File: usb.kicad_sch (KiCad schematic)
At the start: 20 parts, among them J201 1054500101, Q201 S8050, Q202 S8050, U201 CH340G, U202 CP2104, Y201 Crystal_GND24

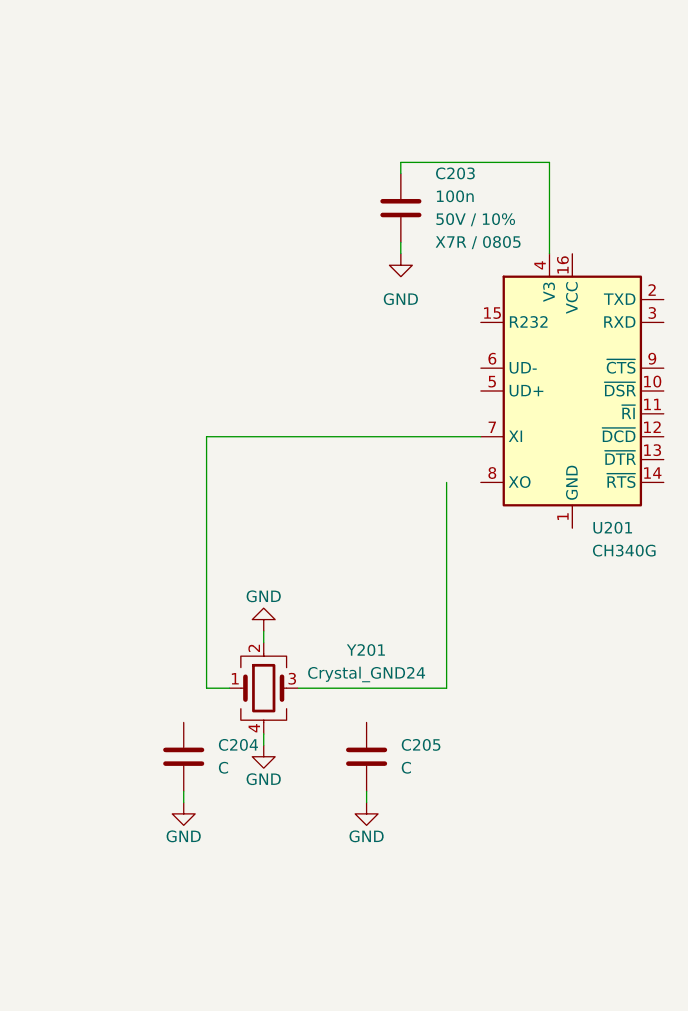
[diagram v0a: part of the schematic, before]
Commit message: Remove CH340G
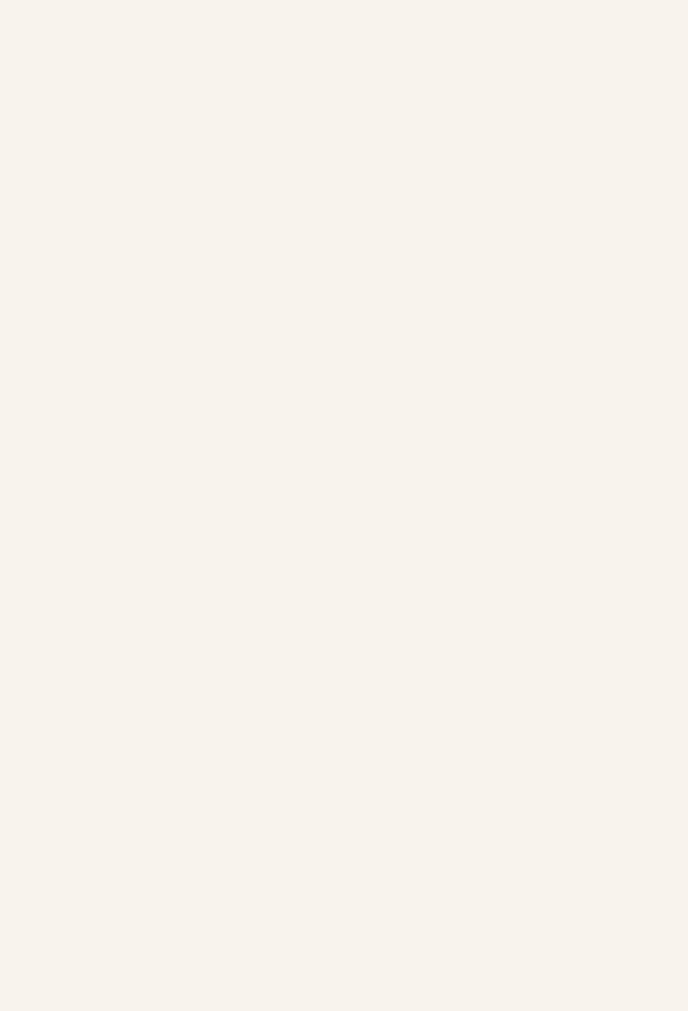
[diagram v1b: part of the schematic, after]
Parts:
- removed C203: 100n, Capacitor_SMD:C_0805_2012Metric, symbol Device:C
- removed C204, C205: C, symbol Device:C
- removed U201: CH340G, Package_SO:SOIC-16_3.9x9.9mm_P1.27mm, symbol Interface_USB:CH340G
- removed Y201: Crystal_GND24, symbol Device:Crystal_GND24

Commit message: Switch to 16 pin USB-C
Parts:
- removed C207: 4u7, Capacitor_SMD:C_0805_2012Metric, symbol Device:C_Small
- C201, C202, C208: symbol Device:C -> Device:C_Small
- J201: value 1054500101 -> GT-USB-7010ASV; footprint busbuddy:USB_C_Receptacle_Molex_105450-0101 -> busbuddy:USB_C_Receptacle_G-Switch_GT-USB-7010ASV; LCSC Part Number C134092 -> C2988369; MPN MOLEX -> G-Switch; Manufacturer 1054500101 -> GT-USB-7010ASV
- R201, R202, R203, R204: symbol Device:R -> Device:R_Small
- R205: footprint (none) -> Resistor_SMD:R_0805_2012Metric
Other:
- moved on the sheet: Q201, R201, R202, R203, R204

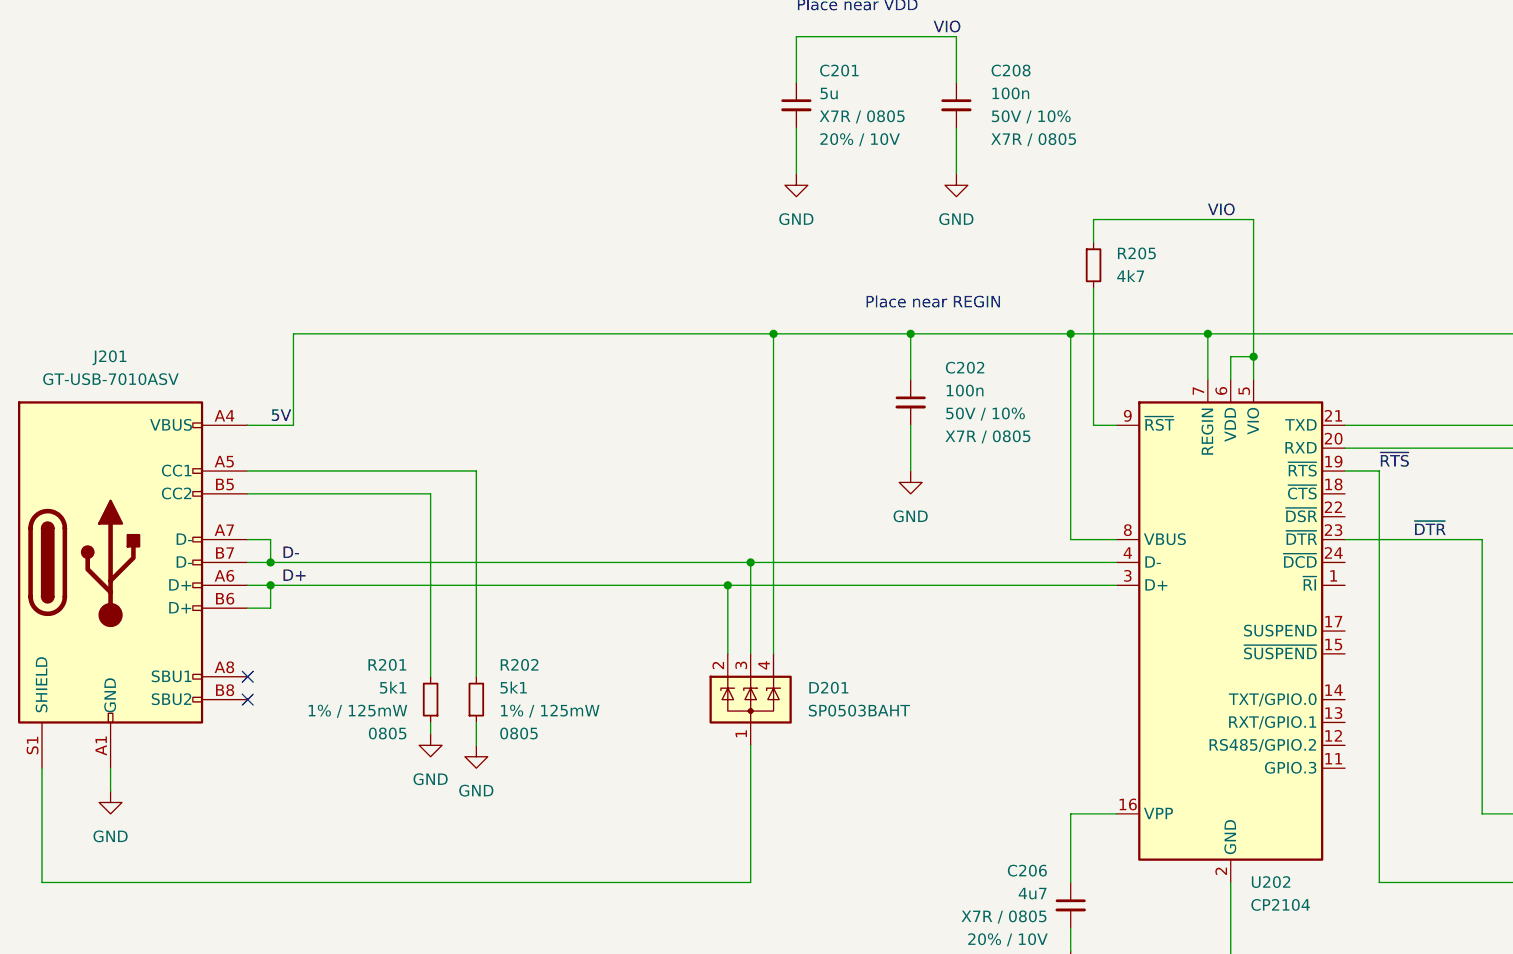
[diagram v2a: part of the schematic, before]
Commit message: Correct SPI pinout
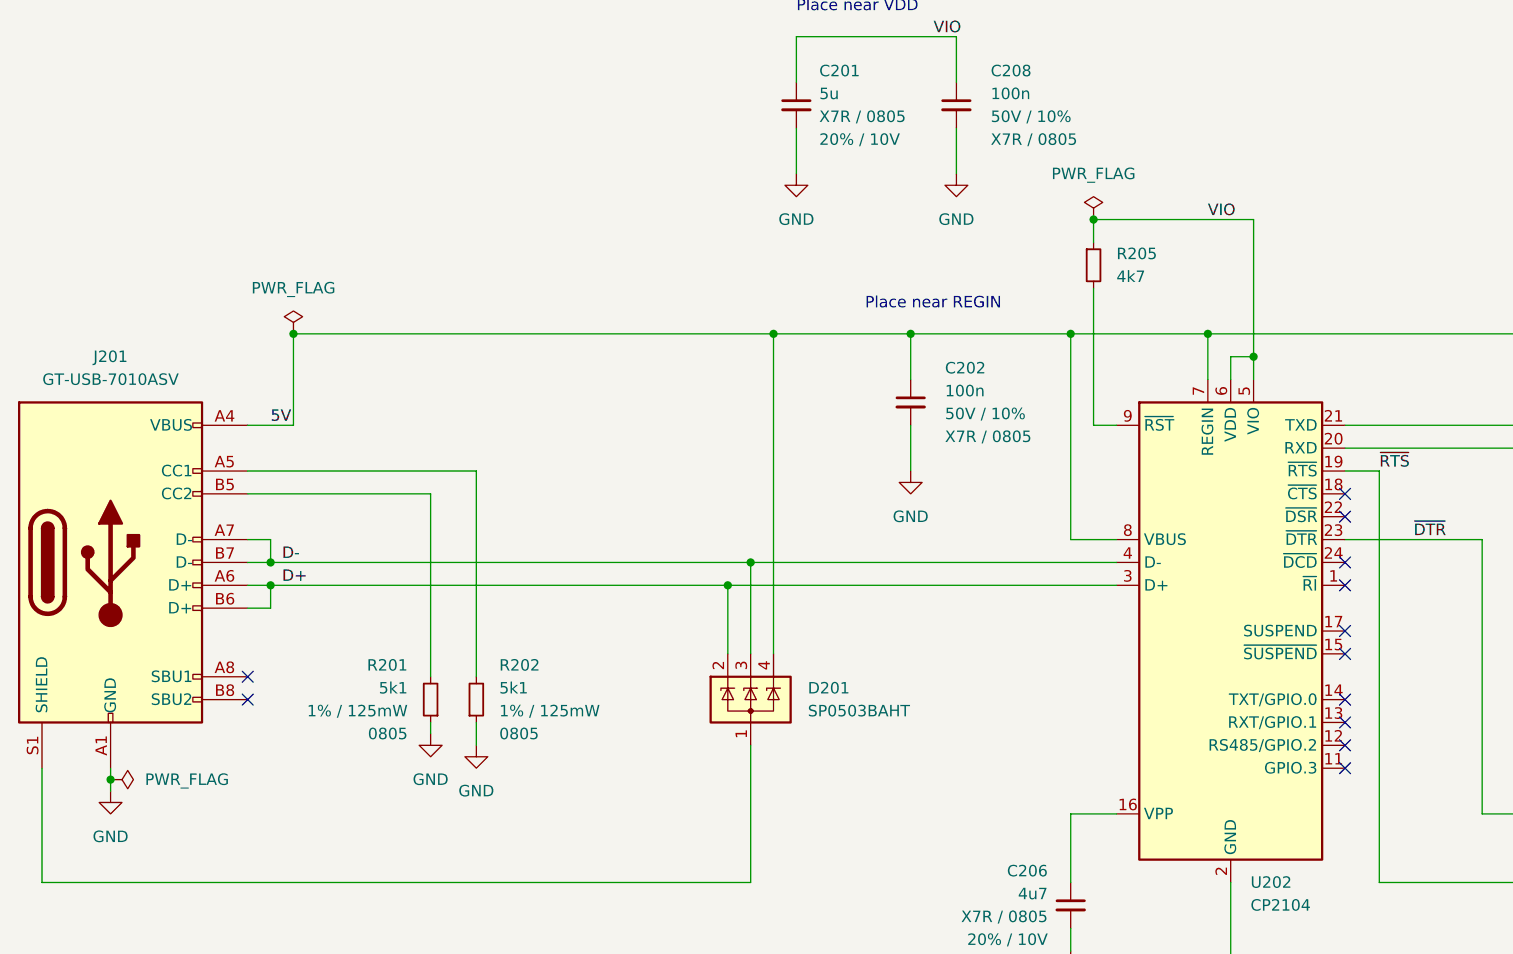
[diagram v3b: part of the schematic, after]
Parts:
- J201: symbol Connector:USB_C_Receptacle_USB2.0 -> Connector:USB_C_Receptacle_USB2.0_16P
- Q201, Q202: footprint Package_TO_SOT_SMD:SOT-23 -> Package_TO_SOT_SMD:SOT-23-3
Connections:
- no-connect marks 2 -> 12

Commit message: Finish everything
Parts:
- C201: value 5u -> 4u7; LCSC Part Number C5189822 -> C98192; MPN CS2012X7R106M100NRE -> CL21A475KBQNNNE; Manufacturer Samwha Capacitor -> Samsung Electro-Mechanics; Rated Voltage 10V -> 50V; Tolerance 20% -> 10%
- C206: LCSC Part Number C5189822 -> C98192; MPN CS2012X7R106M100NRE -> CL21A475KBQNNNE; Manufacturer Samwha Capacitor -> Samsung Electro-Mechanics; Rated Voltage 10V -> 50V; Tolerance 20% -> 10%
- D201: LCSC Part Number (none) -> C7074; MPN (none) -> SP0503BAHTG; Manufacturer (none) -> Littelfuse
- R205: LCSC Part Number (none) -> C17673; MPN (none) -> 0805W8F4701T5E; Manufacturer (none) -> UNI-ROYAL(Uniroyal Elec)
- U202: LCSC Part Number (none) -> C47742; MPN (none) -> CP2104-F03-GMR; Manufacturer (none) -> SKYWORKS/SILICON LABS
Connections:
- net D+: now also D201.3 (K); no longer D201.2 (K)
- net D-: now also D201.2 (K); no longer D201.3 (K)
- net CC1: now reaches J201.A5 (CC1), R202.2
- net CC2: now reaches J201.B5 (CC2), R201.2
- net SHIELD: now reaches D201.1 (A), J201.S1 (SHIELD)
- net CP2104_~{RST}: now reaches R205.2, U202.9 (~{RST})
- net VPP: now reaches C206.1, U202.16 (VPP)

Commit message: Rename project
Damn squatters
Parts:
- J201: footprint busbuddy:USB_C_Receptacle_G-Switch_GT-USB-7010ASV -> youdbetterrun:USB_C_Receptacle_G-Switch_GT-USB-7010ASV
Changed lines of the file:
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@@
 		)
 		(instances
-			(project "busbuddy"
+			(project "youdbetterrun"
 				(path "/50da2b4e-34b1-4787-8ee6-5d7d17f804f4/951b5697-f1e3-4d2e-841e-7032f41eb35f"
 					(reference "#FLG03")
@@
 			)
 		)
-		(property "Footprint" "busbuddy:USB_C_Receptacle_G-Switch_GT-USB-7010ASV"
+		(property "Footprint" "youdbetterrun:USB_C_Receptacle_G-Switch_GT-USB-7010ASV"
 			(at 54.61 76.2 0)
 			(effects
@@
 		)
 		(instances
-			(project "busbuddy"
+			(project "youdbetterrun"
 				(path "/50da2b4e-34b1-4787-8ee6-5d7d17f804f4/951b5697-f1e3-4d2e-841e-7032f41eb35f"
 					(reference "J201")
@@
 		)
 		(instances
-			(project "busbuddy"
+			(project "youdbetterrun"
 				(path "/50da2b4e-34b1-4787-8ee6-5d7d17f804f4/951b5697-f1e3-4d2e-841e-7032f41eb35f"
 					(reference "Q202")
@@
 		)
 		(instances
-			(project "busbuddy"
+			(project "youdbetterrun"
 				(path "/50da2b4e-34b1-4787-8ee6-5d7d17f804f4/951b5697-f1e3-4d2e-841e-7032f41eb35f"
 					(reference "R202")
@@
 		)
 		(instances
-			(project "busbuddy"
+			(project "youdbetterrun"
 				(path "/50da2b4e-34b1-4787-8ee6-5d7d17f804f4/951b5697-f1e3-4d2e-841e-7032f41eb35f"
 					(reference "#FLG02")
@@
 		)
 		(instances
-			(project "busbuddy"
+			(project "youdbetterrun"
 				(path "/50da2b4e-34b1-4787-8ee6-5d7d17f804f4/951b5697-f1e3-4d2e-841e-7032f41eb35f"
 					(reference "#PWR0206")
@@
 		)
 		(instances
-			(project "busbuddy"
+			(project "youdbetterrun"
 				(path "/50da2b4e-34b1-4787-8ee6-5d7d17f804f4/951b5697-f1e3-4d2e-841e-7032f41eb35f"
 					(reference "#PWR0207")
@@
 		)
 		(instances
-			(project "busbuddy"
+			(project "youdbetterrun"
 				(path "/50da2b4e-34b1-4787-8ee6-5d7d17f804f4/951b5697-f1e3-4d2e-841e-7032f41eb35f"
 					(reference "C208")
@@
 		)
 		(instances
-			(project "busbuddy"
+			(project "youdbetterrun"
 				(path "/50da2b4e-34b1-4787-8ee6-5d7d17f804f4/951b5697-f1e3-4d2e-841e-7032f41eb35f"
 					(reference "#PWR0213")
@@
 		)
 		(instances
-			(project "busbuddy"
+			(project "youdbetterrun"
 				(path "/50da2b4e-34b1-4787-8ee6-5d7d17f804f4/951b5697-f1e3-4d2e-841e-7032f41eb35f"
 					(reference "R205")
@@
 		)
 		(instances
-			(project "busbuddy"
+			(project "youdbetterrun"
 				(path "/50da2b4e-34b1-4787-8ee6-5d7d17f804f4/951b5697-f1e3-4d2e-841e-7032f41eb35f"
 					(reference "R203")
@@
 		)
 		(instances
-			(project "busbuddy"
+			(project "youdbetterrun"
 				(path "/50da2b4e-34b1-4787-8ee6-5d7d17f804f4/951b5697-f1e3-4d2e-841e-7032f41eb35f"
 					(reference "#PWR0212")
@@
 		)
 		(instances
-			(project "busbuddy"
+			(project "youdbetterrun"
 				(path "/50da2b4e-34b1-4787-8ee6-5d7d17f804f4/951b5697-f1e3-4d2e-841e-7032f41eb35f"
 					(reference "C206")
@@
 		)
 		(instances
-			(project "busbuddy"
+			(project "youdbetterrun"
 				(path "/50da2b4e-34b1-4787-8ee6-5d7d17f804f4/951b5697-f1e3-4d2e-841e-7032f41eb35f"
 					(reference "C201")
@@
 		)
 		(instances
-			(project "busbuddy"
+			(project "youdbetterrun"
 				(path "/50da2b4e-34b1-4787-8ee6-5d7d17f804f4/951b5697-f1e3-4d2e-841e-7032f41eb35f"
 					(reference "U202")
@@
 		)
 		(instances
-			(project "busbuddy"
+			(project "youdbetterrun"
 				(path "/50da2b4e-34b1-4787-8ee6-5d7d17f804f4/951b5697-f1e3-4d2e-841e-7032f41eb35f"
 					(reference "R204")
@@
 		)
 		(instances
-			(project "busbuddy"
+			(project "youdbetterrun"
 				(path "/50da2b4e-34b1-4787-8ee6-5d7d17f804f4/951b5697-f1e3-4d2e-841e-7032f41eb35f"
 					(reference "D201")
@@
 		)
 		(instances
-			(project "busbuddy"
+			(project "youdbetterrun"
 				(path "/50da2b4e-34b1-4787-8ee6-5d7d17f804f4/951b5697-f1e3-4d2e-841e-7032f41eb35f"
 					(reference "R201")
@@
 		)
 		(instances
-			(project "busbuddy"
+			(project "youdbetterrun"
 				(path "/50da2b4e-34b1-4787-8ee6-5d7d17f804f4/951b5697-f1e3-4d2e-841e-7032f41eb35f"
 					(reference "#FLG01")
@@
 		)
 		(instances
-			(project "busbuddy"
+			(project "youdbetterrun"
 				(path "/50da2b4e-34b1-4787-8ee6-5d7d17f804f4/951b5697-f1e3-4d2e-841e-7032f41eb35f"
 					(reference "#PWR0202")
@@
 		)
 		(instances
-			(project "busbuddy"
+			(project "youdbetterrun"
 				(path "/50da2b4e-34b1-4787-8ee6-5d7d17f804f4/951b5697-f1e3-4d2e-841e-7032f41eb35f"
 					(reference "C202")
@@
 		)
 		(instances
-			(project "busbuddy"
+			(project "youdbetterrun"
 				(path "/50da2b4e-34b1-4787-8ee6-5d7d17f804f4/951b5697-f1e3-4d2e-841e-7032f41eb35f"
 					(reference "#PWR0205")
@@
 		)
 		(instances
-			(project "busbuddy"
+			(project "youdbetterrun"
 				(path "/50da2b4e-34b1-4787-8ee6-5d7d17f804f4/951b5697-f1e3-4d2e-841e-7032f41eb35f"
 					(reference "Q201")
@@
 		)
 		(instances
-			(project "busbuddy"
+			(project "youdbetterrun"
 				(path "/50da2b4e-34b1-4787-8ee6-5d7d17f804f4/951b5697-f1e3-4d2e-841e-7032f41eb35f"
 					(reference "#PWR0201")
@@
 		)
 		(instances
-			(project "busbuddy"
+			(project "youdbetterrun"
 				(path "/50da2b4e-34b1-4787-8ee6-5d7d17f804f4/951b5697-f1e3-4d2e-841e-7032f41eb35f"
 					(reference "#PWR0204")
